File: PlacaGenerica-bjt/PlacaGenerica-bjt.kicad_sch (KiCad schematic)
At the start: 13 parts, among them J1 Screw_Terminal_01x01, J2 Screw_Terminal_01x01, J3 Screw_Terminal_01x01, J4 Screw_Terminal_01x01, Q1 BC337

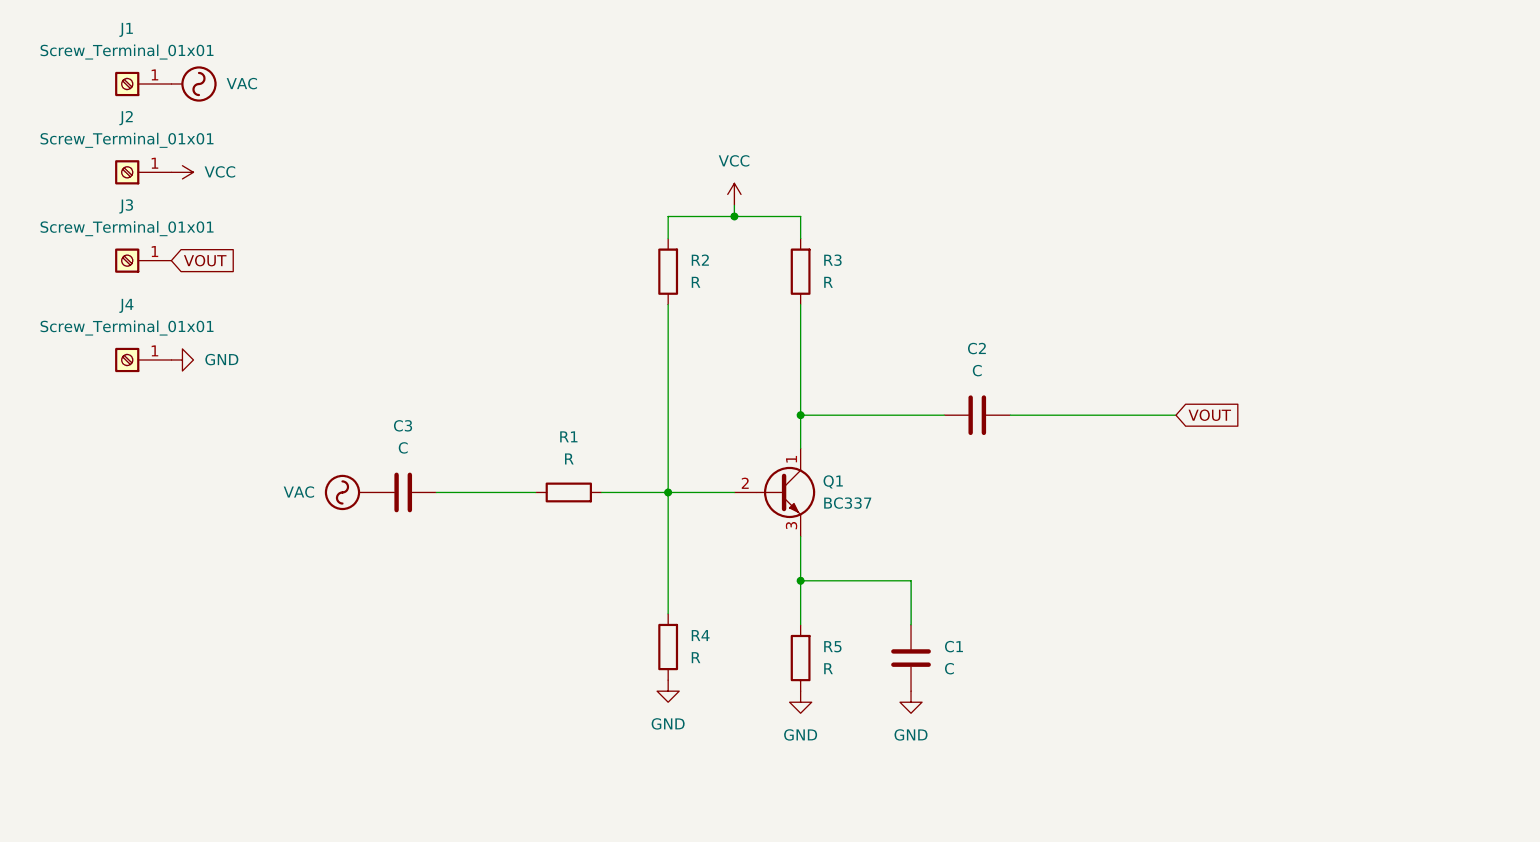
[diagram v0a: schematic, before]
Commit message: Actualiza PlacaGenerica-bjt para todos los lab
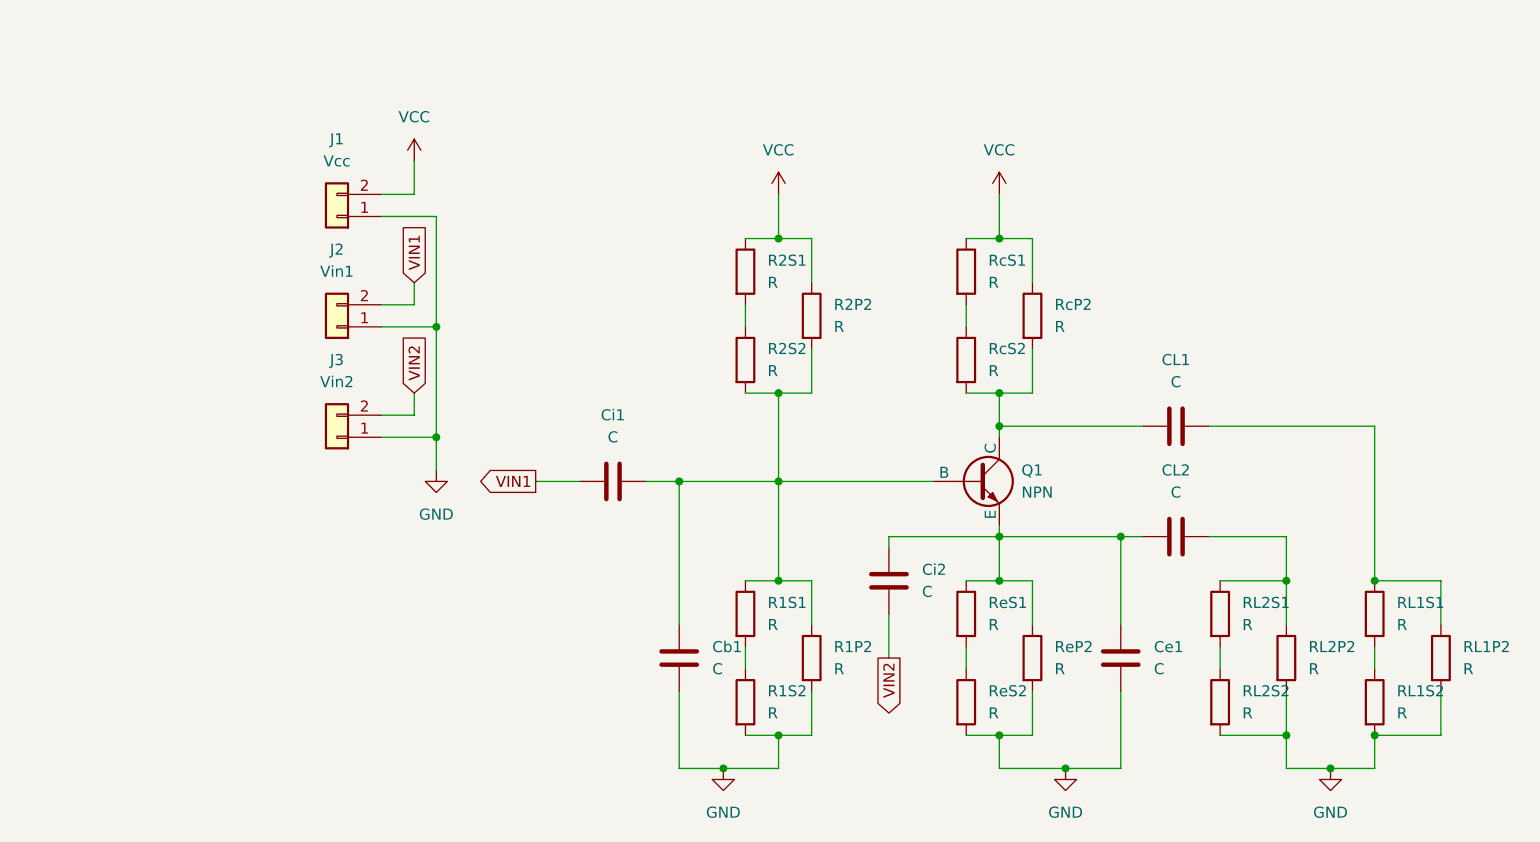
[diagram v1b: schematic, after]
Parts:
- removed C1, C2, C3: C, Capacitor_THT:C_Disc_D4.7mm_W2.5mm_P5.00mm, symbol Device:C
- removed J1, J2, J3, J4: Screw_Terminal_01x01, TestPoint:TestPoint_Pad_4.0x4.0mm, symbol Connector:Screw_Terminal_01x01
- removed Q1: BC337, Package_TO_SOT_THT:TO-92L_Wide, symbol Transistor_BJT:BC337
- removed R1, R2, R3, R4, R5: R, Resistor_THT:R_Axial_DIN0207_L6.3mm_D2.5mm_P10.16mm_Horizontal, symbol Device:R
- added CL1, CL2, Cb1, Ce1, Ci1, Ci2: C, Capacitor_THT:C_Disc_D5.0mm_W2.5mm_P5.00mm, symbol Device:C
- added J1: Vcc, TestPoint:TestPoint_2Pads_Pitch5.08mm_Drill1.3mm, symbol Connector_Generic:Conn_01x02
- added J2: Vin1, TestPoint:TestPoint_2Pads_Pitch5.08mm_Drill1.3mm, symbol Connector_Generic:Conn_01x02
- added J3: Vin2, TestPoint:TestPoint_2Pads_Pitch5.08mm_Drill1.3mm, symbol Connector_Generic:Conn_01x02
- added Q1: NPN, Package_TO_SOT_THT:TO-92_Wide, symbol Simulation_SPICE:NPN
- added R1P2, R1S1, R1S2, R2P2, R2S1, R2S2, RL1P2, RL1S1, RL1S2, RL2P2, RL2S1, RL2S2, RcP2, RcS1, RcS2, ReP2, ReS1, ReS2: R, Resistor_THT:R_Axial_DIN0207_L6.3mm_D2.5mm_P7.62mm_Horizontal, symbol Device:R
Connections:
- net GND: now also Cb1.2, Ce1.2, J1.1 (Pin_1), J2.1 (Pin_1), J3.1 (Pin_1), R1P2.2, R1S2.2, RL1P2.2, RL1S2.2, RL2P2.2, RL2S2.2, ReP2.2, ReS2.2
- net VCC: now also J1.2 (Pin_2), R2P2.1, R2S1.1, RcP2.1, RcS1.1
- new net: Cb1.1, Ci1.2, Q1.2 (B), R1P2.1, R1S1.1, R2P2.2, R2S2.2
- new net: CL1.2, RL1P2.1, RL1S1.1
- new net: RL1S1.2, RL1S2.1
- new net: R1S1.2, R1S2.1
- new net: CL2.1, Ce1.1, Ci2.1, Q1.3 (E), ReP2.1, ReS1.1
- new net: ReS1.2, ReS2.1
- new net: CL1.1, Q1.1 (C), RcP2.2, RcS2.2
- new net: CL2.2, RL2P2.1, RL2S1.1
- new net: RL2S1.2, RL2S2.1
- new net: R2S1.2, R2S2.1
- new net: RcS1.2, RcS2.1
- new net VIN1: Ci1.1, J2.2 (Pin_2)
- new net VIN2: Ci2.2, J3.2 (Pin_2)

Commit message: Agrega serigrafia visual a PlacaGenerica-bjt
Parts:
- CL1, CL2, Cb1, Ce1, Ci1, Ci2: footprint Capacitor_THT:C_Disc_D5.0mm_W2.5mm_P5.00mm -> PrettyFootprints:Pretty-C_Disc_D5.0mm_W2.5mm_P5.00mm
- Q1: footprint Package_TO_SOT_THT:TO-92_Wide -> PrettyFootprints:Pretty-TO-92_Wide
- R1P2, R1S1, R1S2, R2P2, R2S1, R2S2, RL1P2, RL1S1, RL1S2, RL2P2, RL2S1, RL2S2, RcP2, RcS1, RcS2, ReP2, ReS1, ReS2: footprint Resistor_THT:R_Axial_DIN0207_L6.3mm_D2.5mm_P7.62mm_Horizontal -> PrettyFootprints:Pretty-R_Axial_DIN0207_L6.3mm_D2.5mm_P7.62mm_Horizontal
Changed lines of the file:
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@@
 			)
 		)
-		(property "Footprint" "Resistor_THT:R_Axial_DIN0207_L6.3mm_D2.5mm_P7.62mm_Horizontal"
+		(property "Footprint" "PrettyFootprints:Pretty-R_Axial_DIN0207_L6.3mm_D2.5mm_P7.62mm_Horizontal"
 			(at 134.112 69.85 90)
 			(effects
@@
 			)
 		)
-		(property "Footprint" "Capacitor_THT:C_Disc_D5.0mm_W2.5mm_P5.00mm"
+		(property "Footprint" "PrettyFootprints:Pretty-C_Disc_D5.0mm_W2.5mm_P5.00mm"
 			(at 116.84 87.9348 0)
 			(effects
@@
 			)
 		)
-		(property "Footprint" "Resistor_THT:R_Axial_DIN0207_L6.3mm_D2.5mm_P7.62mm_Horizontal"
+		(property "Footprint" "PrettyFootprints:Pretty-R_Axial_DIN0207_L6.3mm_D2.5mm_P7.62mm_Horizontal"
 			(at 198.882 104.14 90)
 			(effects
@@
 			)
 		)
-		(property "Footprint" "Resistor_THT:R_Axial_DIN0207_L6.3mm_D2.5mm_P7.62mm_Horizontal"
+		(property "Footprint" "PrettyFootprints:Pretty-R_Axial_DIN0207_L6.3mm_D2.5mm_P7.62mm_Horizontal"
 			(at 126.492 104.14 90)
 			(effects
@@
 			)
 		)
-		(property "Footprint" "Resistor_THT:R_Axial_DIN0207_L6.3mm_D2.5mm_P7.62mm_Horizontal"
+		(property "Footprint" "PrettyFootprints:Pretty-R_Axial_DIN0207_L6.3mm_D2.5mm_P7.62mm_Horizontal"
 			(at 151.892 104.14 90)
 			(effects
@@
 			)
 		)
-		(property "Footprint" "Resistor_THT:R_Axial_DIN0207_L6.3mm_D2.5mm_P7.62mm_Horizontal"
+		(property "Footprint" "PrettyFootprints:Pretty-R_Axial_DIN0207_L6.3mm_D2.5mm_P7.62mm_Horizontal"
 			(at 159.512 109.22 90)
 			(effects
@@
 			)
 		)
-		(property "Footprint" "Capacitor_THT:C_Disc_D5.0mm_W2.5mm_P5.00mm"
+		(property "Footprint" "PrettyFootprints:Pretty-C_Disc_D5.0mm_W2.5mm_P5.00mm"
 			(at 181.61 81.5848 0)
 			(effects
@@
 			)
 		)
-		(property "Footprint" "Capacitor_THT:C_Disc_D5.0mm_W2.5mm_P5.00mm"
+		(property "Footprint" "PrettyFootprints:Pretty-C_Disc_D5.0mm_W2.5mm_P5.00mm"
 			(at 172.4152 113.03 0)
 			(effects
@@
 			)
 		)
-		(property "Footprint" "Resistor_THT:R_Axial_DIN0207_L6.3mm_D2.5mm_P7.62mm_Horizontal"
+		(property "Footprint" "PrettyFootprints:Pretty-R_Axial_DIN0207_L6.3mm_D2.5mm_P7.62mm_Horizontal"
 			(at 198.882 114.3 90)
 			(effects
@@
 			)
 		)
-		(property "Footprint" "Capacitor_THT:C_Disc_D5.0mm_W2.5mm_P5.00mm"
+		(property "Footprint" "PrettyFootprints:Pretty-C_Disc_D5.0mm_W2.5mm_P5.00mm"
 			(at 181.61 94.2848 0)
 			(effects
@@
 			)
 		)
-		(property "Footprint" "Resistor_THT:R_Axial_DIN0207_L6.3mm_D2.5mm_P7.62mm_Horizontal"
+		(property "Footprint" "PrettyFootprints:Pretty-R_Axial_DIN0207_L6.3mm_D2.5mm_P7.62mm_Horizontal"
 			(at 181.102 104.14 90)
 			(effects
@@
 			)
 		)
-		(property "Footprint" "Resistor_THT:R_Axial_DIN0207_L6.3mm_D2.5mm_P7.62mm_Horizontal"
+		(property "Footprint" "PrettyFootprints:Pretty-R_Axial_DIN0207_L6.3mm_D2.5mm_P7.62mm_Horizontal"
 			(at 126.492 74.93 90)
 			(effects
@@
 			)
 		)
-		(property "Footprint" "Resistor_THT:R_Axial_DIN0207_L6.3mm_D2.5mm_P7.62mm_Horizontal"
+		(property "Footprint" "PrettyFootprints:Pretty-R_Axial_DIN0207_L6.3mm_D2.5mm_P7.62mm_Horizontal"
 			(at 206.502 109.22 90)
 			(effects
@@
 			)
 		)
-		(property "Footprint" "Resistor_THT:R_Axial_DIN0207_L6.3mm_D2.5mm_P7.62mm_Horizontal"
+		(property "Footprint" "PrettyFootprints:Pretty-R_Axial_DIN0207_L6.3mm_D2.5mm_P7.62mm_Horizontal"
 			(at 188.722 109.22 90)
 			(effects
@@
 			)
 		)
-		(property "Footprint" "Resistor_THT:R_Axial_DIN0207_L6.3mm_D2.5mm_P7.62mm_Horizontal"
+		(property "Footprint" "PrettyFootprints:Pretty-R_Axial_DIN0207_L6.3mm_D2.5mm_P7.62mm_Horizontal"
 			(at 134.112 109.22 90)
 			(effects
@@
 			)
 		)
-		(property "Footprint" "Package_TO_SOT_THT:TO-92_Wide"
+		(property "Footprint" "PrettyFootprints:Pretty-TO-92_Wide"
 			(at 218.44 88.9 0)
 			(effects
@@
 			)
 		)
-		(property "Footprint" "Resistor_THT:R_Axial_DIN0207_L6.3mm_D2.5mm_P7.62mm_Horizontal"
+		(property "Footprint" "PrettyFootprints:Pretty-R_Axial_DIN0207_L6.3mm_D2.5mm_P7.62mm_Horizontal"
 			(at 151.892 114.3 90)
 			(effects
@@
 			)
 		)
-		(property "Footprint" "Resistor_THT:R_Axial_DIN0207_L6.3mm_D2.5mm_P7.62mm_Horizontal"
+		(property "Footprint" "PrettyFootprints:Pretty-R_Axial_DIN0207_L6.3mm_D2.5mm_P7.62mm_Horizontal"
 			(at 159.512 69.85 90)
 			(effects
@@
 			)
 		)
-		(property "Footprint" "Capacitor_THT:C_Disc_D5.0mm_W2.5mm_P5.00mm"
+		(property "Footprint" "PrettyFootprints:Pretty-C_Disc_D5.0mm_W2.5mm_P5.00mm"
 			(at 145.7452 104.14 0)
 			(effects
@@
 			)
 		)
-		(property "Footprint" "Resistor_THT:R_Axial_DIN0207_L6.3mm_D2.5mm_P7.62mm_Horizontal"
+		(property "Footprint" "PrettyFootprints:Pretty-R_Axial_DIN0207_L6.3mm_D2.5mm_P7.62mm_Horizontal"
 			(at 126.492 64.77 90)
 			(effects
@@
 			)
 		)
-		(property "Footprint" "Capacitor_THT:C_Disc_D5.0mm_W2.5mm_P5.00mm"
+		(property "Footprint" "PrettyFootprints:Pretty-C_Disc_D5.0mm_W2.5mm_P5.00mm"
 			(at 121.6152 113.03 0)
 			(effects
@@
 			)
 		)
-		(property "Footprint" "Resistor_THT:R_Axial_DIN0207_L6.3mm_D2.5mm_P7.62mm_Horizontal"
+		(property "Footprint" "PrettyFootprints:Pretty-R_Axial_DIN0207_L6.3mm_D2.5mm_P7.62mm_Horizontal"
 			(at 151.892 64.77 90)
 			(effects
@@
 			)
 		)
-		(property "Footprint" "Resistor_THT:R_Axial_DIN0207_L6.3mm_D2.5mm_P7.62mm_Horizontal"
+		(property "Footprint" "PrettyFootprints:Pretty-R_Axial_DIN0207_L6.3mm_D2.5mm_P7.62mm_Horizontal"
 			(at 181.102 114.3 90)
 			(effects
@@
 			)
 		)
-		(property "Footprint" "Resistor_THT:R_Axial_DIN0207_L6.3mm_D2.5mm_P7.62mm_Horizontal"
+		(property "Footprint" "PrettyFootprints:Pretty-R_Axial_DIN0207_L6.3mm_D2.5mm_P7.62mm_Horizontal"
 			(at 126.492 114.3 90)
 			(effects
@@
 			)
 		)
-		(property "Footprint" "Resistor_THT:R_Axial_DIN0207_L6.3mm_D2.5mm_P7.62mm_Horizontal"
+		(property "Footprint" "PrettyFootprints:Pretty-R_Axial_DIN0207_L6.3mm_D2.5mm_P7.62mm_Horizontal"
 			(at 151.892 74.93 90)
 			(effects
